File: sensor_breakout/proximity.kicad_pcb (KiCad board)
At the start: 2 copper layers, 12.6 x 16.5 mm, 9 parts, among them IC1 VL53L4CDV0DH_1, J4 Conn_01x05

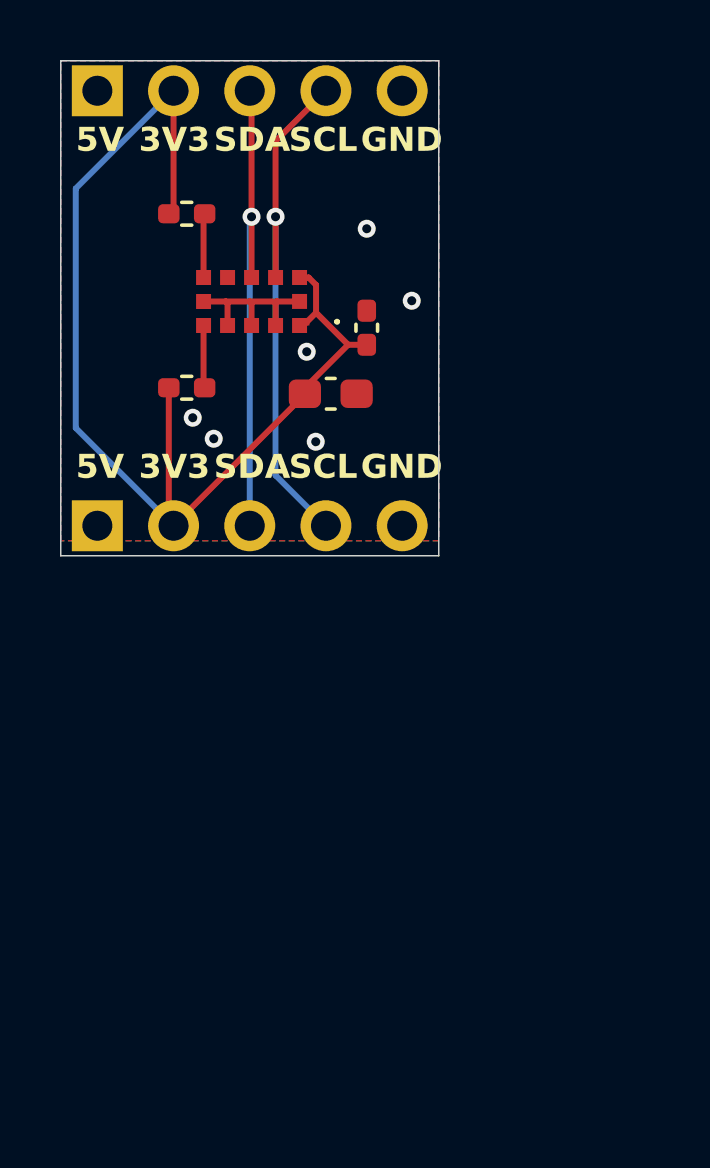
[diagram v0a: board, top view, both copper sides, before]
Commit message: add caps to host; make sensor_breakouts larger; update bom & generated production files for everything
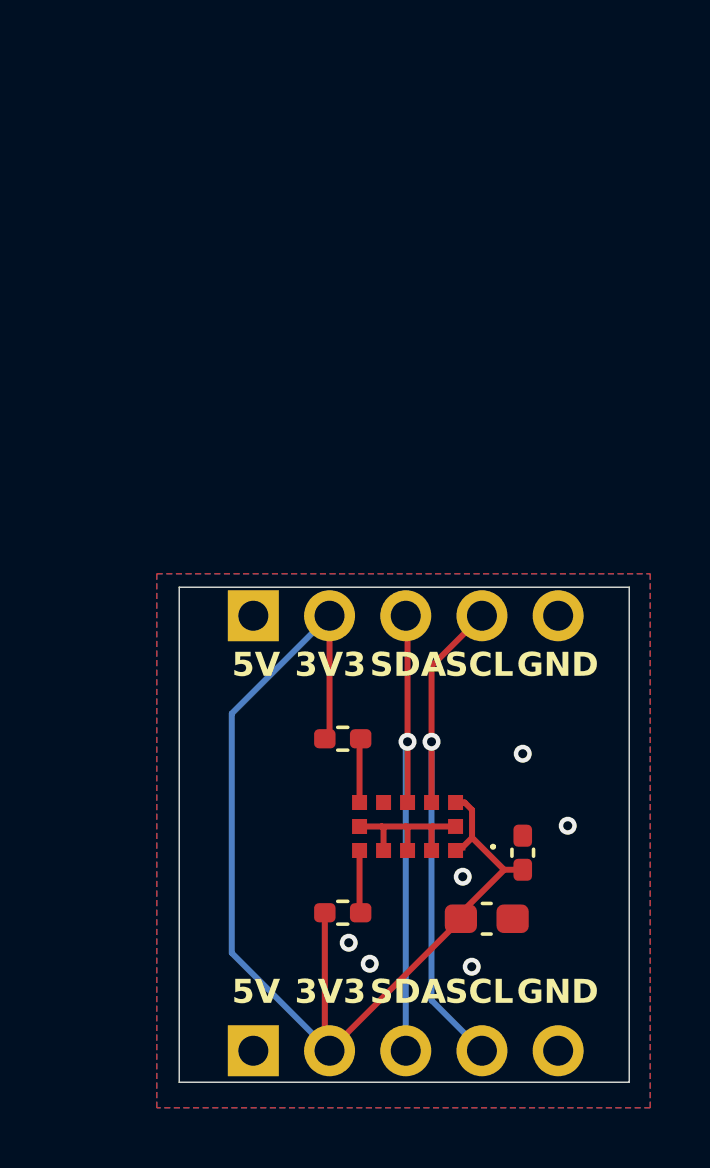
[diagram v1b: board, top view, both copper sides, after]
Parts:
- removed the G*** at (119.3, 95.7)
- removed the G*** at (117.7, 90.9)
- removed the J4 at (116.3, 87.6)
- removed the J4 at (116.3, 102.1)
- added G***: LOGO, LOGO, B.Cu at (124.5, 113.2)
- added G***: LOGO, LOGO, B.Cu at (122.9, 108.4)
- added J4: Conn_01x05, Connector_PinHeader_2.54mm:PinHeader_1x05_P2.54mm_Vertical, F.Cu at (121.5, 119.6)
- added J4: Conn_01x05, Connector_PinHeader_2.54mm:PinHeader_1x05_P2.54mm_Vertical, F.Cu at (121.5, 105.1)
- moved C12 18.3 mm to (129.3, 115.2)
- moved C11 18.3 mm to (130.5, 113.0)
- moved IC1 18.3 mm to (126.7, 112.1)
- moved R20 18.3 mm to (124.5, 109.2)
- moved R21 18.3 mm to (124.5, 115.0)
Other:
- board size 12.6 x 16.5 mm -> 15 x 16.5 mm
